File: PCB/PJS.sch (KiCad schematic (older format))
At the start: 40 parts, among them J1 HFW8R-1STE1H1LF_FFC, J10 SM02B-PASS-TBT_Connector, J2 SM02B-PASS-TBT_Connector, J3 SM02B-PASS-TBT_Connector, J4 SM02B-PASS-TBT_Connector, J5 SM02B-PASS-TBT_Connector, J6 SM02B-PASS-TBT_Connector, J7 SM02B-PASS-TBT_Connector, J8 SM02B-PASS-TBT_Connector, J9 SM02B-PASS-TBT_Connector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

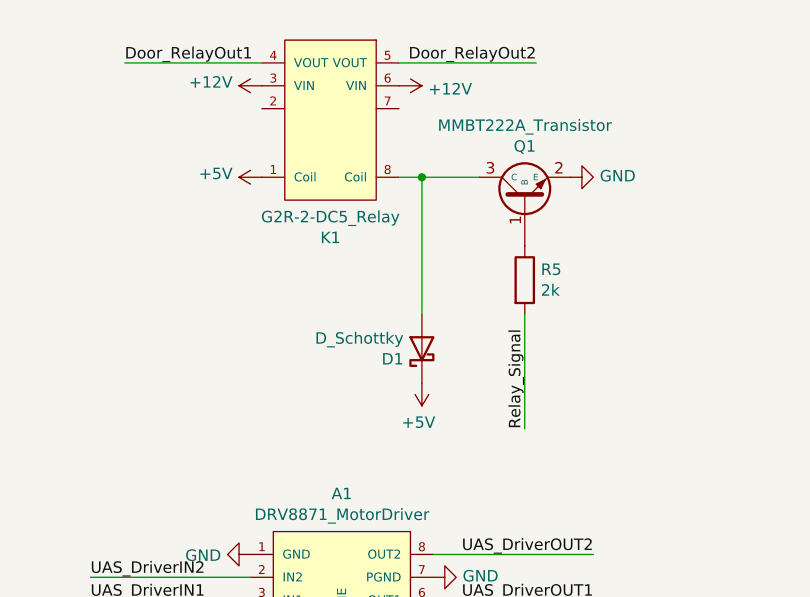
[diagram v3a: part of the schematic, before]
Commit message: Finished PCB
All traces are sized and spaced. The XT60 and relay pins are fixed.
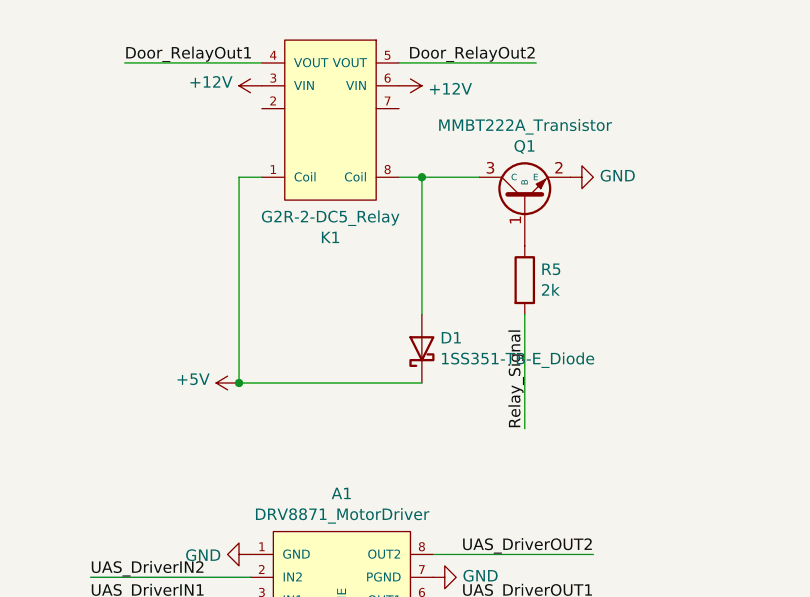
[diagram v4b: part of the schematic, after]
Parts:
- removed D1: D_Schottky, PJS:1SS351-TB-E_Diode, symbol Device:D_Schottky
- added D1: 1SS351-TB-E_Diode, symbol PJS:1SS351-TB-E_Diode
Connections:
- net +5V: now also D1.3 (K)
- net at K1.8 (Coil), Q1.3 (C): now also D1.1 (A)
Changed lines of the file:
@@
 	1900 1350 1300 1350
-$Comp
-L power:+5V #PWR0155
-U 1 1 5FF0D0F3
-P 1900 1850
-F 0 "#PWR0155" H 1900 1700 50  0001 C CNN
-F 1 "+5V" V 1915 1978 50  0000 L CNN
-F 2 "" H 1900 1850 50  0001 C CNN
-F 3 "" H 1900 1850 50  0001 C CNN
-	1    1900 1850
-	0    -1   -1   0
-$EndComp
-$Comp
-L power:+5V #PWR0154
-U 1 1 5FF0C5F2
-P 2600 2750
-F 0 "#PWR0154" H 2600 2600 50  0001 C CNN
-F 1 "+5V" H 2615 2923 50  0000 C CNN
-F 2 "" H 2600 2750 50  0001 C CNN
-F 3 "" H 2600 2750 50  0001 C CNN
-	1    2600 2750
-	-1   0    0    1
-$EndComp
 $Comp
 L power:GND #PWR0122
@@
 	0    -1   -1   0
 $EndComp
-$Comp
-L Device:D_Schottky D1
-U 1 1 5FFF832A
-P 2600 2600
-F 0 "D1" V 2554 2680 50  0000 L CNN
-F 1 "D_Schottky" V 2645 2680 50  0000 L CNN
-F 2 "PJS:1SS351-TB-E_Diode" H 2600 2600 50  0001 C CNN
-F 3 "~" H 2600 2600 50  0001 C CNN
-	1    2600 2600
-	0    -1   -1   0
-$EndComp
-Wire Wire Line
-	2600 1850 2600 2450
 Wire Wire Line
 	2600 1850 2500 1850
@@
 Connection ~ 12850 1350
 Connection ~ 10850 1800
+Wire Wire Line
+	2600 1850 2600 2450
+Wire Wire Line
+	1800 1850 1800 2750
+Wire Wire Line
+	1800 2750 2600 2750
+Wire Wire Line
+	1800 1850 1900 1850
+$Comp
+L power:+5V #PWR0154
+U 1 1 60053597
+P 1800 2750
+F 0 "#PWR0154" H 1800 2600 50  0001 C CNN
+F 1 "+5V" V 1815 2878 50  0000 L CNN
+F 2 "" H 1800 2750 50  0001 C CNN
+F 3 "" H 1800 2750 50  0001 C CNN
+	1    1800 2750
+	0    -1   -1   0
+$EndComp
+Connection ~ 1800 2750
+$Comp
+L PJS:1SS351-TB-E_Diode D1
+U 1 1 600E996D
+P 2600 2600
+F 0 "D1" V 2646 2520 50  0000 R CNN
+F 1 "1SS351-TB-E_Diode" V 2555 2520 50  0000 R CNN
+F 2 "" H 2600 2600 50  0001 C CNN
+F 3 "" H 2600 2600 50  0001 C CNN
+	1    2600 2600
+	0    -1   -1   0
+$EndComp
 $EndSCHEMATC
